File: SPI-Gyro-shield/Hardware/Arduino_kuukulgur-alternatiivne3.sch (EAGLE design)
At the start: 171 parts, among them IC2 TPS77301DGK, IC4 CP2103_USB_UART, T1 BD651, U1 MPU-6000QFN-24, U2 txb0108, X2 USBSMD, Y1 CSTCE8M00G15C99-R0

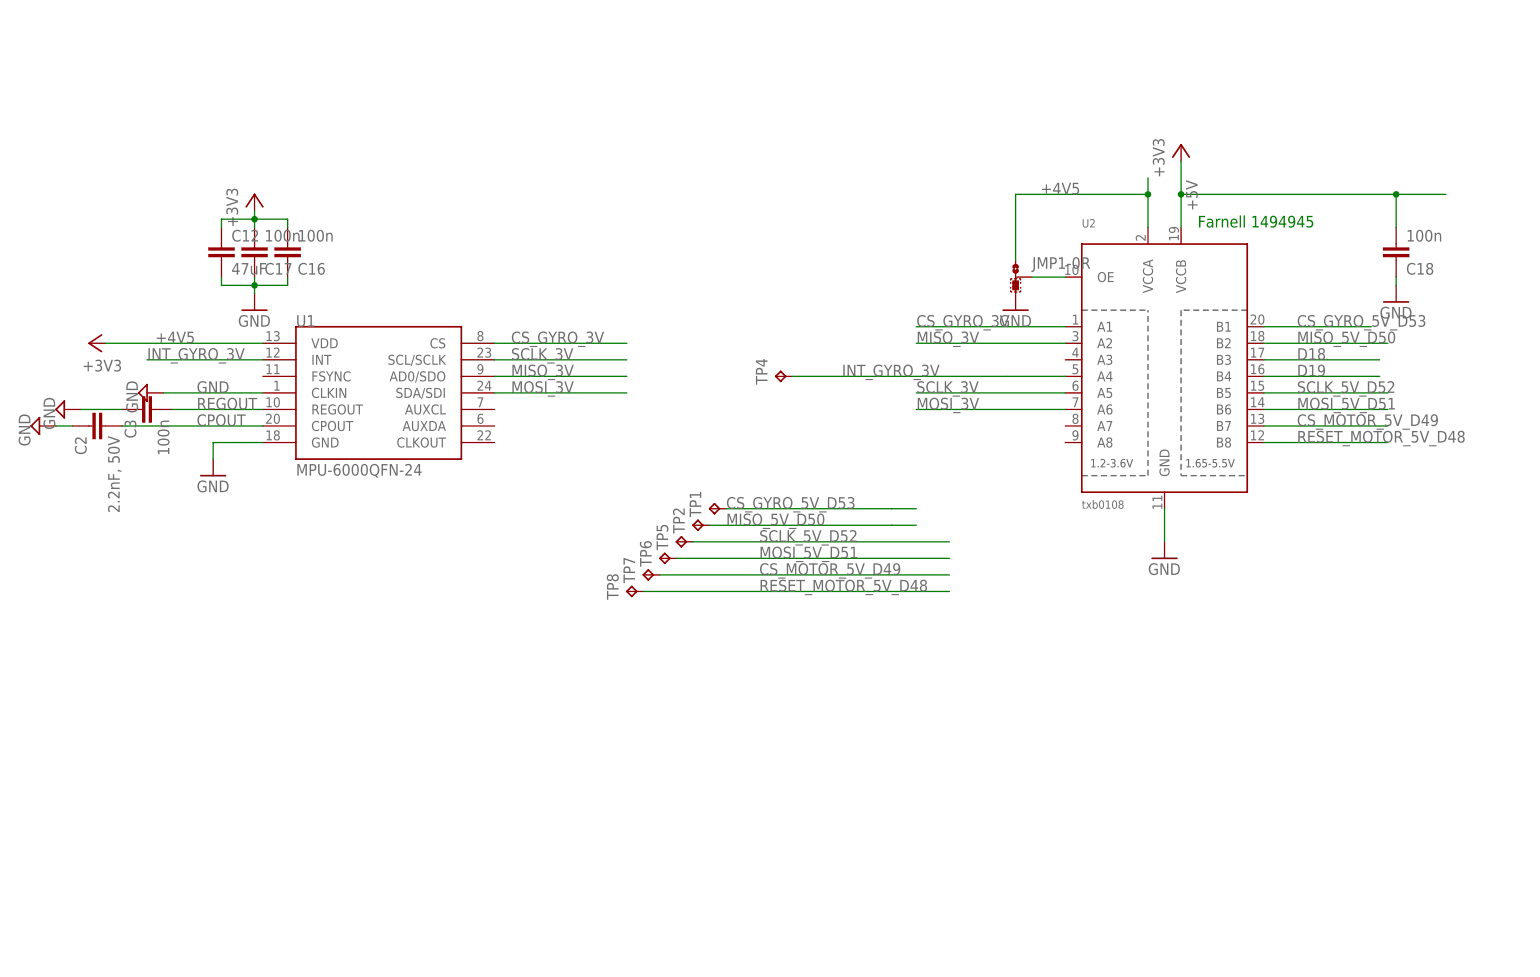
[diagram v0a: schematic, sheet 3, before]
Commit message: Shield PCB as ordered in.
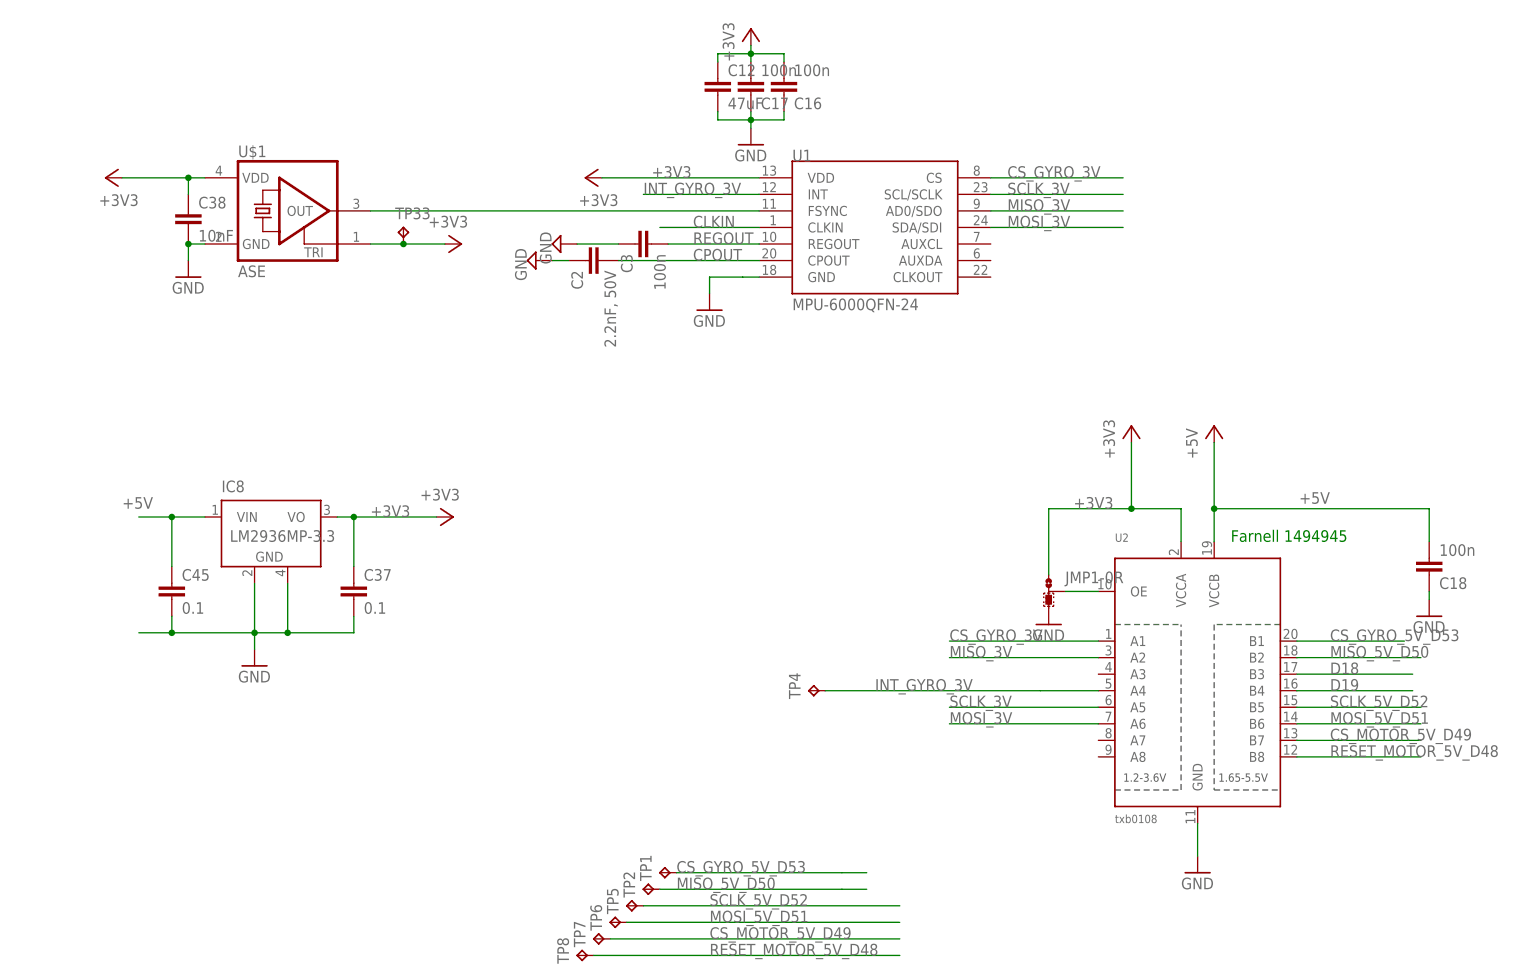
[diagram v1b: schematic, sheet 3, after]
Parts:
- removed TP34: TPB1,27, testpad:TPB1,27
- added C34, C35: 1uF/6V, resistor:C-EUC0603
- added C36: 100uF/6V, rcl:CPOL-EUC/6032-28R
- added C37, C45: 0.1, SparkFun:CAP0603-CAP
- added C38: 10nF, rcl:C-EUC0603
- added IC1: TPS77333DGK, samuel:TPS773
- added IC8: LM2936MP-3.3, national-semiconductor:LM2936MP-3.0
- added TP3: TPB1,27, testpad:TPB1,27
- added U$1: ASE, crystal:ASE
- C29: value 100uF/16V -> 100uF/6V
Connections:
- removed net _CLK2: MCU.P72/CLK2/TA1OUT/V, R23.1, TP22.TP
- removed net _MISO2: MCU.P71/RXD2/SCL2/TA0IN/TB5IN/SX2, MOTOR2.7, R21.1, R22.2, R33.2, TP24.TP
- removed net _MOSI2: MCU.P70/TXD2/SDA2/TA0OUT/SRX2, R20.1, R32.2, TP23.TP
- new net +3V3: C12.1, C16.2, C17.2, C33.1, C34.1, C36.+, C37.1, C38.1, IC1.FB\SENSE, IC1.OUT@1, IC1.OUT@2, IC4.VDD, IC4.VIO, IC8.VO, JMP1-0R.1, JP3.8, TP33.TP, U$1.TRI, U$1.VDD, U1.VDD, U2.VCCA
- new net CLKIN: U1.CLKIN
- new net N$108: MCU.P70/TXD2/SDA2/TA0OUT/SRX2, R32.2
- new net N$135: MCU.P71/RXD2/SCL2/TA0IN/TB5IN/SX2, R33.2
- new net N$165: MCU.P72/CLK2/TA1OUT/V, TP3.TP
- new net N$166: U$1.OUT, U1.FSYNC
- new net _CLK6: MCU.P45/CS2/A21/CLK6, R23.1, TP22.TP
- new net _MISO6: MOTOR2.7, R21.1, R22.2, TP24.TP
- new net _MISO６: MCU.P46/CS1/A22/RX6
- new net _MOSI6: MCU.P47/CS0/A23/TX6, R20.1, TP23.TP
- net +4V5: no longer C12.1, C16.2, C17.2, C33.1, IC4.VDD, IC4.VIO, JMP1-0R.1, U1.VDD, U2.VCCA
- net +5V: now also C35.1, C45.1, IC1.IN@1, IC1.IN@2, IC8.VIN
- net GND: now also C34.2, C35.2, C36.-, C37.2, C38.2, C45.2, IC1.!EN, IC1.GND, IC8.GND@1, IC8.GND@2, U$1.GND; no longer U1.CLKIN
- net RX3: no longer MCU.P47/CS0/A23/TX6, TP33.TP
- net TX3: no longer MCU.P46/CS1/A22/RX6, TP34.TP
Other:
- moved on the sheet: C12, C16, C17, C18, C2, C26, C28, C29, C3, IC2, JMP1-0R, R48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

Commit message: PCB updates
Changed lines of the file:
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@@
 <net name="SCLK_3V" class="0">
 <segment>
-<wire x1="132.08" y1="15.24" x2="109.22" y2="15.24" width="0.1524" layer="91"/>
-<label x="109.22" y="15.24" size="1.778" layer="95"/>
+<wire x1="132.08" y1="15.24" x2="104.14" y2="15.24" width="0.1524" layer="91"/>
+<label x="104.14" y="15.24" size="1.778" layer="95"/>
 <pinref part="U2" gate="G$1" pin="A5"/>
 </segment>
@@
 <net name="MOSI_3V" class="0">
 <segment>
-<wire x1="132.08" y1="12.7" x2="109.22" y2="12.7" width="0.1524" layer="91"/>
-<label x="109.22" y="12.7" size="1.778" layer="95"/>
+<wire x1="132.08" y1="12.7" x2="104.14" y2="12.7" width="0.1524" layer="91"/>
+<label x="104.14" y="12.7" size="1.778" layer="95"/>
 <pinref part="U2" gate="G$1" pin="A6"/>
 </segment>
@@
 <net name="MISO_3V" class="0">
 <segment>
-<wire x1="132.08" y1="22.86" x2="109.22" y2="22.86" width="0.1524" layer="91"/>
-<label x="109.22" y="22.86" size="1.778" layer="95"/>
+<wire x1="132.08" y1="22.86" x2="104.14" y2="22.86" width="0.1524" layer="91"/>
+<label x="104.14" y="22.86" size="1.778" layer="95"/>
 <pinref part="U2" gate="G$1" pin="A2"/>
 </segment>
@@
 <net name="CS_GYRO_3V" class="0">
 <segment>
-<wire x1="132.08" y1="25.4" x2="109.22" y2="25.4" width="0.1524" layer="91"/>
-<label x="109.22" y="25.4" size="1.778" layer="95"/>
+<wire x1="132.08" y1="25.4" x2="104.14" y2="25.4" width="0.1524" layer="91"/>
+<label x="104.14" y="25.4" size="1.778" layer="95"/>
 <pinref part="U2" gate="G$1" pin="A1"/>
 </segment>
@@
 <segment>
 <wire x1="110.49" y1="57.15" x2="107.95" y2="57.15" width="0.1524" layer="91"/>
-<label x="102.362" y="56.134" size="1.778" layer="95"/>
+<label x="82.042" y="56.134" size="1.778" layer="95"/>
 <pinref part="JP8" gate="G$1" pin="3"/>
 </segment>
@@
 <segment>
 <wire x1="110.49" y1="59.69" x2="107.95" y2="59.69" width="0.1524" layer="91"/>
-<label x="102.362" y="58.674" size="1.778" layer="95"/>
+<label x="82.042" y="58.674" size="1.778" layer="95"/>
 <pinref part="JP8" gate="G$1" pin="2"/>
 </segment>
@@
 <segment>
 <wire x1="110.49" y1="62.23" x2="107.95" y2="62.23" width="0.1524" layer="91"/>
-<label x="102.362" y="61.214" size="1.778" layer="95"/>
+<label x="82.042" y="61.214" size="1.778" layer="95"/>
 <pinref part="JP8" gate="G$1" pin="1"/>
 </segment>

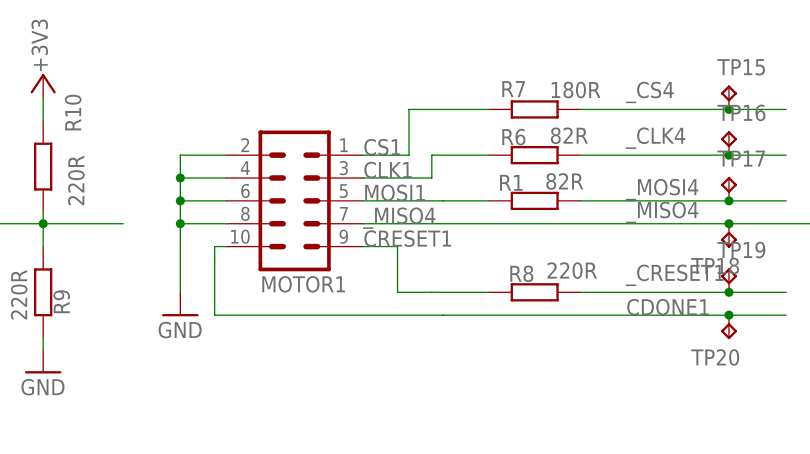
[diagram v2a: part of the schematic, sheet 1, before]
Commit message: Misc schematic clarifications
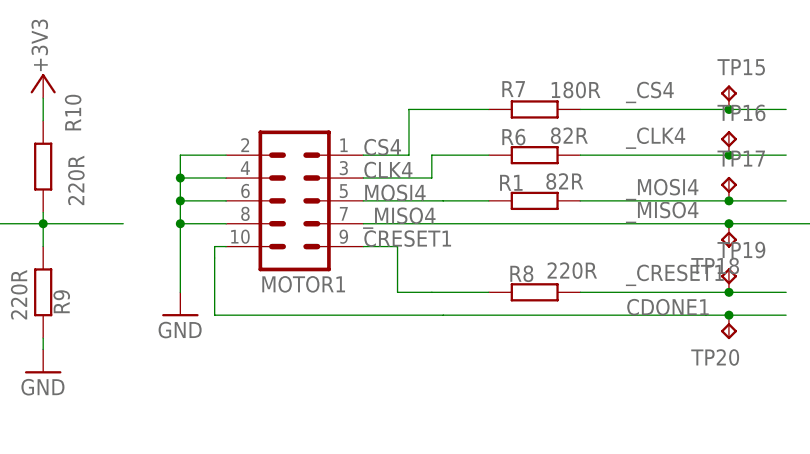
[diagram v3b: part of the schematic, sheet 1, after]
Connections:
- net CLK1 renamed CLK4
- net CS1 renamed CS4
- net MOSI1 renamed MOSI4
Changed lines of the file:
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@@
 </segment>
 </net>
-<net name="CS1" class="0">
+<net name="CS4" class="0">
 <segment>
 <pinref part="MOTOR1" gate="G$1" pin="1"/>
@@
 </segment>
 </net>
-<net name="CLK1" class="0">
+<net name="CLK4" class="0">
 <segment>
 <pinref part="MOTOR1" gate="G$1" pin="3"/>
@@
 </segment>
 </net>
-<net name="MOSI1" class="0">
+<net name="MOSI4" class="0">
 <segment>
 <pinref part="MOTOR1" gate="G$1" pin="5"/>
